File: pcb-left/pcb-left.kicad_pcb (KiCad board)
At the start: 2 copper layers, 124.8 x 104.5 mm, 43 parts, among them J1 BAT, U1 xiao-ble

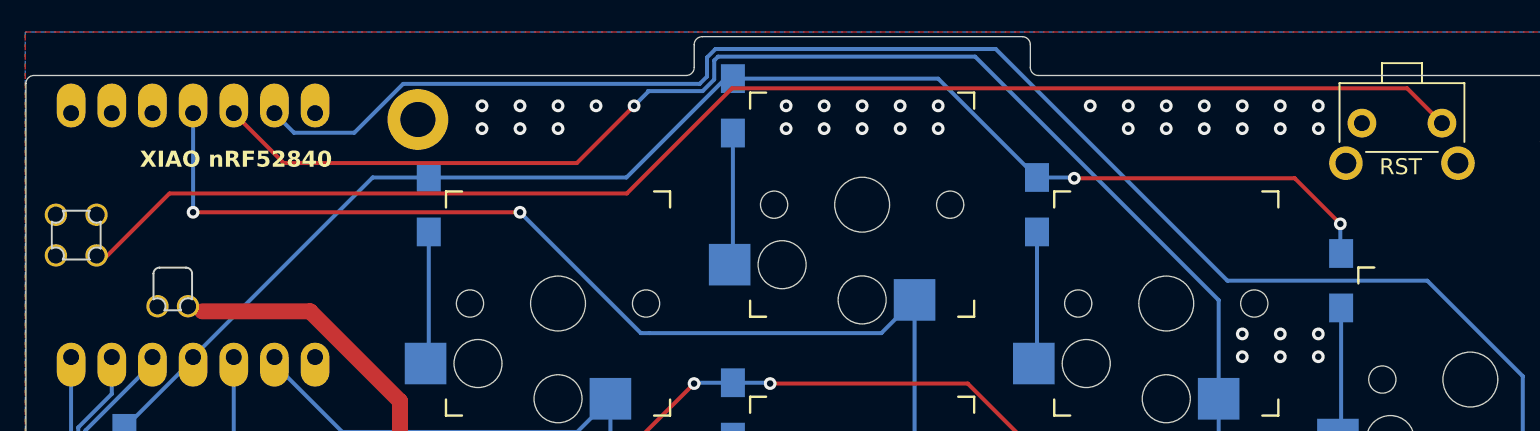
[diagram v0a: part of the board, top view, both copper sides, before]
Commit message: Rename project directories
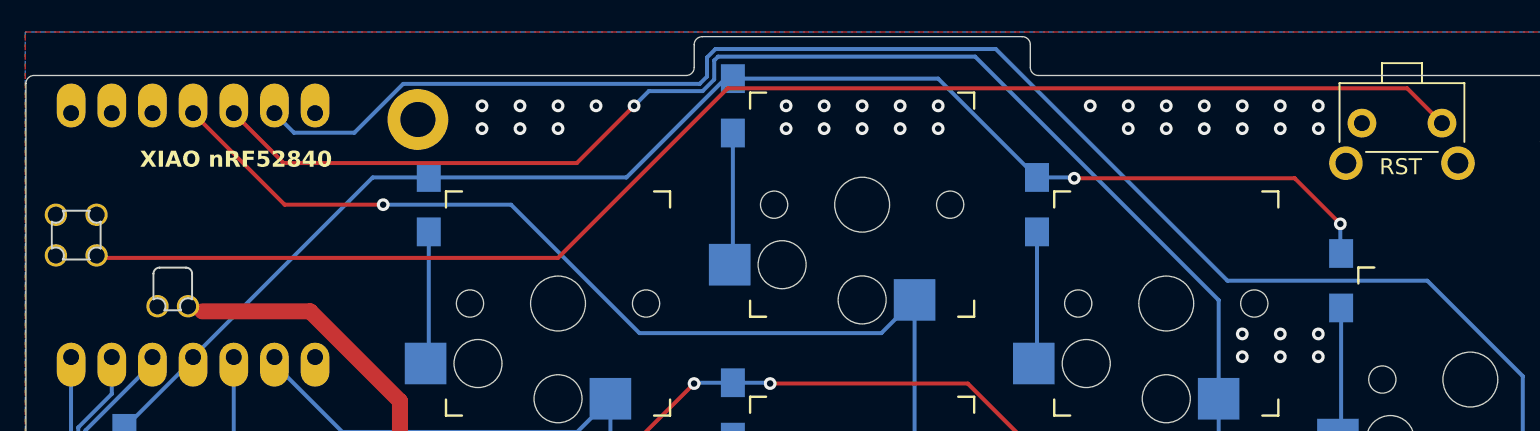
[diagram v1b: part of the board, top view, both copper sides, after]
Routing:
- net COL2_L: track 132.0 -> 128.4 mm, vias 2 -> 1
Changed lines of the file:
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@@
     (grid_origin 90.015625 72.425)
     (pcbplotparams
-      (layerselection 0x0000100_7ffffffe)
+      (layerselection 0x00010fc_ffffffff)
       (plot_on_all_layers_selection 0x0000000_00000000)
       (disableapertmacros false)
@@
       (plotinvisibletext false)
       (sketchpadsonfab false)
-      (subtractmaskfromsilk false)
-      (outputformat 3)
+      (subtractmaskfromsilk true)
+      (outputformat 1)
       (mirror false)
       (drillshape 0)
       (scaleselection 1)
-      (outputdirectory "")
+      (outputdirectory "pcb-left-gerbers/")
     )
   )
@@
     (fp_arc (start -2.5 6.2) (mid -2.146447 6.346447) (end -2 6.7)
       (stroke (width 0.15) (type solid)) (layer "B.SilkS"))
-    (fp_arc (start -1 3.7) (mid -2.06066 3.26066) (end -2.5 2.2)
+    (fp_arc (start -1 3.7) (mid -2.06066 3.260659) (end -2.5 2.2)
       (stroke (width 0.15) (type solid)) (layer "B.SilkS"))
     (fp_line (start -7 -6) (end -7 -7)
@@
     (fp_arc (start -2.5 6.2) (mid -2.146447 6.346447) (end -2 6.7)
       (stroke (width 0.15) (type solid)) (layer "B.Fab"))
-    (fp_arc (start -1 3.7) (mid -2.06066 3.26066) (end -2.5 2.2)
+    (fp_arc (start -1 3.7) (mid -2.06066 3.260659) (end -2.5 2.2)
       (stroke (width 0.15) (type solid)) (layer "B.Fab"))
     (pad "" np_thru_hole circle (at -5.5 0 165) (size 1.7018 1.7018) (drill 1.7018) (layers "*.Cu" "*.Mask"))
@@
   (via (at 94.765625 37.75) (size 0.8) (drill 0.4) (layers "F.Cu" "B.Cu") (free) (net 24))
   (via (at 52.965625 61.5) (size 0.8) (drill 0.4) (layers "F.Cu" "B.Cu") (free) (net 24))
-  (segment (start 81.88593 36.655) (end 124.065625 36.655) (width 0.25) (layer "F.Cu") (net 25))
-  (segment (start 81.88593 36.655) (end 75.31593 43.225) (width 0.25) (layer "F.Cu") (net 25))
-  (segment (start 75.31593 43.225) (end 46.740625 43.225) (width 0.25) (layer "F.Cu") (net 25))
-  (segment (start 124.065625 36.655) (end 126.240625 38.83) (width 0.25) (layer "F.Cu") (net 25))
-  (segment (start 46.740625 43.225) (end 42.731083 47.234542) (width 0.25) (layer "F.Cu") (net 25))
-  (segment (start 42.731083 47.234542) (end 42.38601 47.234542) (width 0.25) (layer "F.Cu") (net 25))
+  (segment (start 124.065625 36.655) (end 81.610625 36.655) (width 0.25) (layer "F.Cu") (net 25))
+  (segment (start 42.338625 47.25) (end 42.276825 47.1882) (width 0.25) (layer "F.Cu") (net 25))
+  (segment (start 71.015625 47.25) (end 42.338625 47.25) (width 0.25) (layer "F.Cu") (net 25))
+  (segment (start 126.240625 38.83) (end 124.065625 36.655) (width 0.25) (layer "F.Cu") (net 25))
+  (segment (start 81.610625 36.655) (end 71.015625 47.25) (width 0.25) (layer "F.Cu") (net 25))
   (segment (start 50.755625 53.445) (end 50.755625 61.031527) (width 0.25) (layer "B.Cu") (net 26))
   (segment (start 55.290625 65.566527) (end 55.290625 71.725) (width 0.25) (layer "B.Cu") (net 26))
@@
   (segment (start 74.290625 75.05) (end 74.290625 94.05) (width 0.25) (layer "B.Cu") (net 27))
   (segment (start 57.540625 58.125) (end 72.215625 58.125) (width 0.25) (layer "B.Cu") (net 27))
-  (segment (start 48.215625 44.4) (end 68.640625 44.4) (width 0.25) (layer "F.Cu") (net 28))
-  (via (at 48.215625 44.4) (size 0.8) (drill 0.4) (layers "F.Cu" "B.Cu") (net 28))
-  (via (at 68.640625 44.4) (size 0.8) (drill 0.4) (layers "F.Cu" "B.Cu") (net 28))
+  (segment (start 53.935625 43.925) (end 60.090625 43.925) (width 0.25) (layer "F.Cu") (net 28))
+  (segment (start 48.215625 38.205) (end 53.935625 43.925) (width 0.25) (layer "F.Cu") (net 28))
+  (via (at 60.090625 43.925) (size 0.8) (drill 0.4) (layers "F.Cu" "B.Cu") (net 28))
   (segment (start 93.290625 93.837158) (end 93.290625 87.875) (width 0.25) (layer "B.Cu") (net 28))
-  (segment (start 91.215625 51.95) (end 93.290625 49.875) (width 0.25) (layer "B.Cu") (net 28))
-  (segment (start 76.715625 51.95) (end 91.215625 51.95) (width 0.25) (layer "B.Cu") (net 28))
-  (segment (start 68.640625 44.4) (end 76.190625 51.95) (width 0.25) (layer "B.Cu") (net 28))
+  (segment (start 68.078467 43.925) (end 76.103467 51.95) (width 0.25) (layer "B.Cu") (net 28))
+  (segment (start 60.090625 43.925) (end 68.078467 43.925) (width 0.25) (layer "B.Cu") (net 28))
+  (segment (start 76.103467 51.95) (end 91.215625 51.95) (width 0.25) (layer "B.Cu") (net 28))
   (segment (start 93.290625 68.875) (end 93.290625 87.875) (width 0.25) (layer "B.Cu") (net 28))
   (segment (start 112.290625 112.837158) (end 93.290625 93.837158) (width 0.25) (layer "B.Cu") (net 28))
   (segment (start 112.290625 118.75) (end 112.290625 112.837158) (width 0.25) (layer "B.Cu") (net 28))
-  (segment (start 48.215625 38.205) (end 48.215625 44.4) (width 0.25) (layer "B.Cu") (net 28))
-  (segment (start 76.190625 51.95) (end 76.715625 51.95) (width 0.25) (layer "B.Cu") (net 28))
+  (segment (start 91.215625 51.95) (end 93.290625 49.875) (width 0.25) (layer "B.Cu") (net 28))
   (segment (start 93.290625 49.875) (end 93.290625 68.875) (width 0.25) (layer "B.Cu") (net 28))
   (segment (start 72.190625 41.325) (end 75.765625 37.75) (width 0.25) (layer "F.Cu") (net 29))
@@
   (segment (start 53.875625 41.325) (end 72.190625 41.325) (width 0.25) (layer "F.Cu") (net 29))
   (via (at 75.765625 37.75) (size 0.8) (drill 0.4) (layers "F.Cu" "B.Cu") (net 29))
-  (segment (start 76.637569 36.878056) (end 75.765625 37.75) (width 0.25) (layer "B.Cu") (net 29))
   (segment (start 112.290625 94.05) (end 112.290625 104.675) (width 0.25) (layer "B.Cu") (net 29))
   (segment (start 81.015625 34.675) (end 97.074098 34.675) (width 0.25) (layer "B.Cu") (net 29))
-  (segment (start 76.637569 36.828553) (end 80.050676 36.828553) (width 0.25) (layer "B.Cu") (net 29))
+  (segment (start 80.050676 36.828553) (end 76.687072 36.828553) (width 0.25) (layer "B.Cu") (net 29))
+  (segment (start 76.687072 36.828553) (end 75.765625 37.75) (width 0.25) (layer "B.Cu") (net 29))
   (segment (start 115.190625 107.575) (end 123.265625 107.575) (width 0.25) (layer "B.Cu") (net 29))
   (segment (start 80.050676 36.828553) (end 80.772427 36.106802) (width 0.25) (layer "B.Cu") (net 29))
@@
   (segment (start 134.190625 110.425) (end 131.064059 122.244891) (width 0.25) (layer "B.Cu") (net 29))
   (segment (start 97.074098 34.675) (end 112.290625 49.891527) (width 0.25) (layer "B.Cu") (net 29))
-  (segment (start 76.637569 36.828553) (end 76.637569 36.878056) (width 0.25) (layer "B.Cu") (net 29))
   (segment (start 98.364873 34.2) (end 112.838973 48.6741) (width 0.25) (layer "B.Cu") (net 30))
   (segment (start 112.838973 48.6741) (end 125.323198 48.6741) (width 0.25) (layer "B.Cu") (net 30))
